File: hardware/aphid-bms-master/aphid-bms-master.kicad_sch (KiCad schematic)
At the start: 5 parts, among them J1 Main, J2 Slaves, J3 ContactorPos, J4 ContactorNeg, J5 ContactorPrecharge

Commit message: Worked on BMS master
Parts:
- added H1, H2, H3, H4: MountingHole, MountingHole:MountingHole_3.2mm_M3, symbol Mechanical:MountingHole
- added JP1: PRIMARY, Jumper:SolderJumper-2_P1.3mm_Open_RoundedPad1.0x1.5mm, symbol Jumper:SolderJumper_2_Open
- added R9: 10k, Resistor_SMD:R_0805_2012Metric, symbol Device:R
- J4, J5: footprint (none) -> Connector_Molex:Molex_Micro-Fit_3.0_43650-0215_1x02_P3.00mm_Vertical
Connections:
- net CAN/CAN1_HIGH: now also J1.4 (Pin_4); no longer J1.5 (Pin_5)
- net CAN/CAN1_LOW: now also J1.5 (Pin_5); no longer J1.4 (Pin_4)
- net CAN/CAN2_LOW: now also J2.4 (Pin_4); no longer J2.2 (Pin_2)
- net GND: now also R9.2
- net Slave Power/SLAVE_5V: now also J2.2 (Pin_2); no longer J2.4 (Pin_4)
- new net +3.3V: JP1.2 (B)
- new net MCU/PRIMARY: JP1.1 (A), R9.1
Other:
- sheet MCU ports: added PRIMARY; removed none
- note added: "Control wheater this is the primary (front) battery or the secondary (rear) battery. Enables having the same PCB and firmware in both."
- note added: "Daisy-chained to all slave boards with isolated CAN-transcievers. This board contains one 120 ohm termination, the last slave board has the other one."
- note added: "Precharge only used in primary (front) battery"
- company: (none) -> https://aphid-ev.se
- title: (none) -> Aphid BMS Master

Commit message: Worked on BMS master layout
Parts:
- H1, H2, H3, H4: footprint MountingHole:MountingHole_3.2mm_M3 -> MountingHole:MountingHole_4.3mm_M4
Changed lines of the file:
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@@
 			)
 		)
-		(property "Footprint" "MountingHole:MountingHole_3.2mm_M3"
+		(property "Footprint" "MountingHole:MountingHole_4.3mm_M4"
 			(at 29.21 158.75 0)
 			(effects
@@
 			)
 		)
-		(property "Footprint" "MountingHole:MountingHole_3.2mm_M3"
+		(property "Footprint" "MountingHole:MountingHole_4.3mm_M4"
 			(at 29.21 173.99 0)
 			(effects
@@
 			)
 		)
-		(property "Footprint" "MountingHole:MountingHole_3.2mm_M3"
+		(property "Footprint" "MountingHole:MountingHole_4.3mm_M4"
 			(at 29.21 168.91 0)
 			(effects
@@
 			)
 		)
-		(property "Footprint" "MountingHole:MountingHole_3.2mm_M3"
+		(property "Footprint" "MountingHole:MountingHole_4.3mm_M4"
 			(at 29.21 163.83 0)
 			(effects

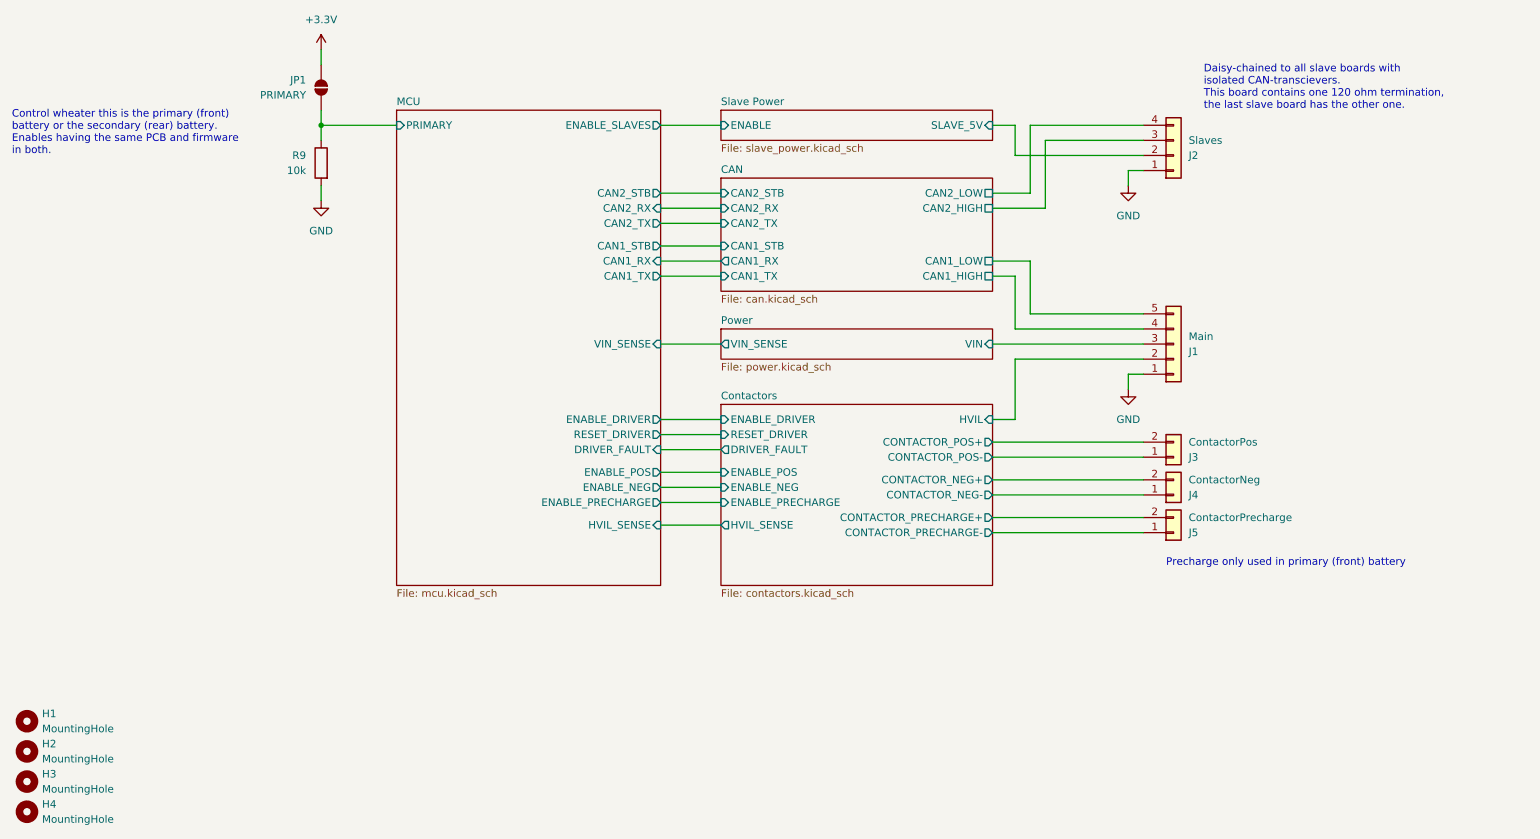
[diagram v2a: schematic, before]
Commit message: Changed BMS Master to use MAX17851 instead of isolated CAN
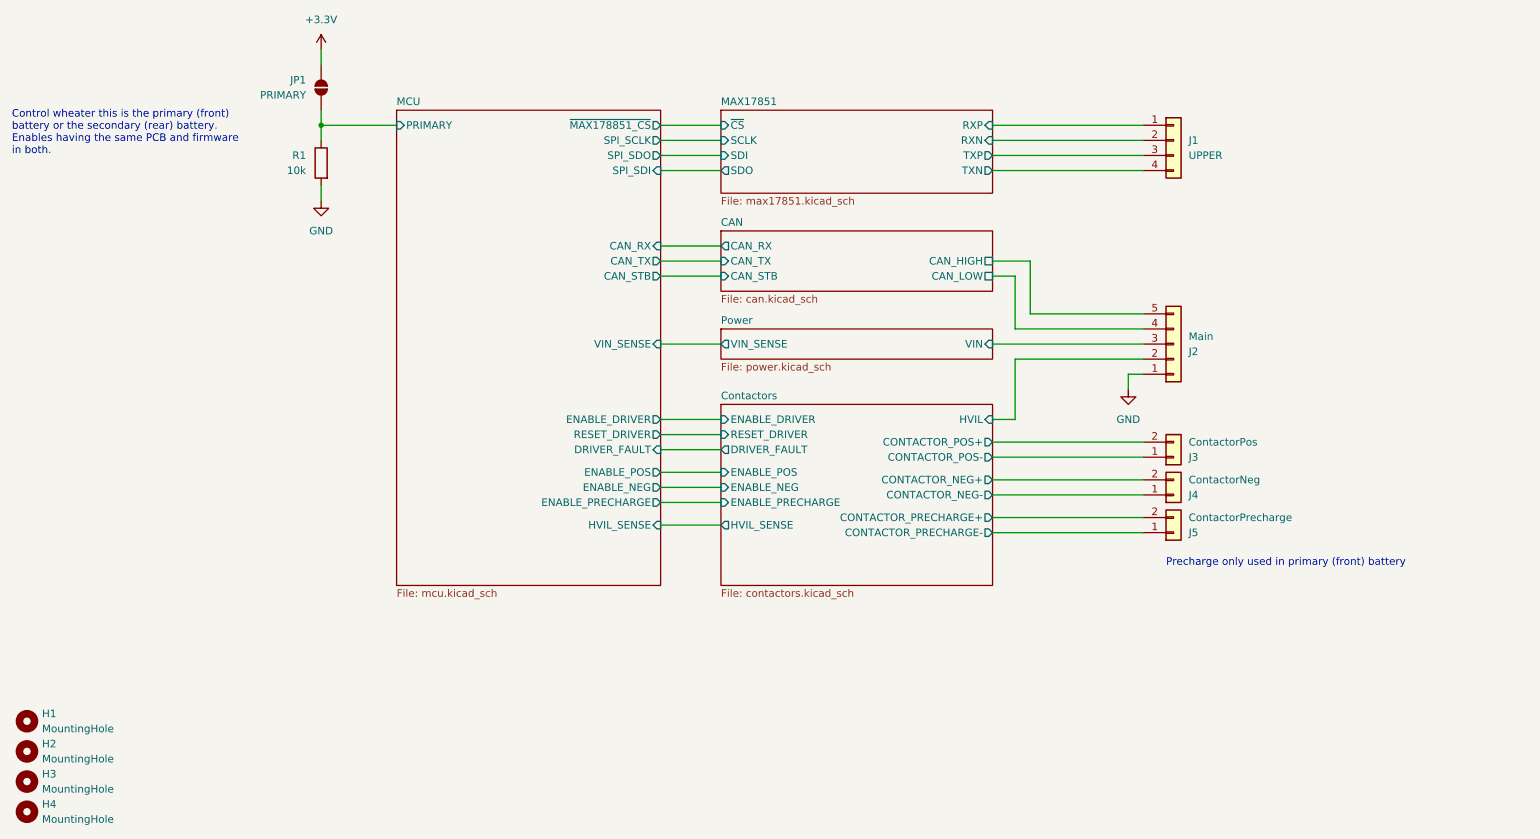
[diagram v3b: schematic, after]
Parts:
- removed J2: Slaves, Connector_Molex:Molex_Micro-Fit_3.0_43045-0412_2x02_P3.00mm_Vertical, symbol Connector_Generic:Conn_01x04
- added J1: UPPER, symbol Connector_Generic:Conn_01x04
- renumbered J1 to J2, R9 to R1
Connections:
- net CAN/CAN1_HIGH renamed CAN/CAN_LOW
- net CAN/CAN1_LOW renamed CAN/CAN_HIGH
- new net MAX17851/RXN: J1.2 (Pin_2)
- new net MAX17851/RXP: J1.1 (Pin_1)
- new net MAX17851/TXN: J1.4 (Pin_4)
- new net MAX17851/TXP: J1.3 (Pin_3)
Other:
- removed sheet Slave Power
- added sheet MAX17851 (max17851.kicad_sch)
- sheet CAN ports: added CAN_HIGH, CAN_LOW, CAN_RX, CAN_STB, CAN_TX; removed CAN1_HIGH, CAN1_LOW, CAN1_RX, CAN1_STB, CAN1_TX, CAN2_HIGH, CAN2_LOW, CAN2_RX, CAN2_STB, CAN2_TX
- sheet MCU ports: added CAN_RX, CAN_STB, CAN_TX, SPI_SCLK, SPI_SDI, SPI_SDO, ~{MAX178851_CS}; removed CAN1_RX, CAN1_STB, CAN1_TX, CAN2_RX, CAN2_STB, CAN2_TX, ENABLE_SLAVES
- note removed: "Daisy-chained to all slave boards with isolated CAN-transcievers. This board contains one 120 ohm termination, the last slave board has the other one."

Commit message: Harmonized VC and BMS components
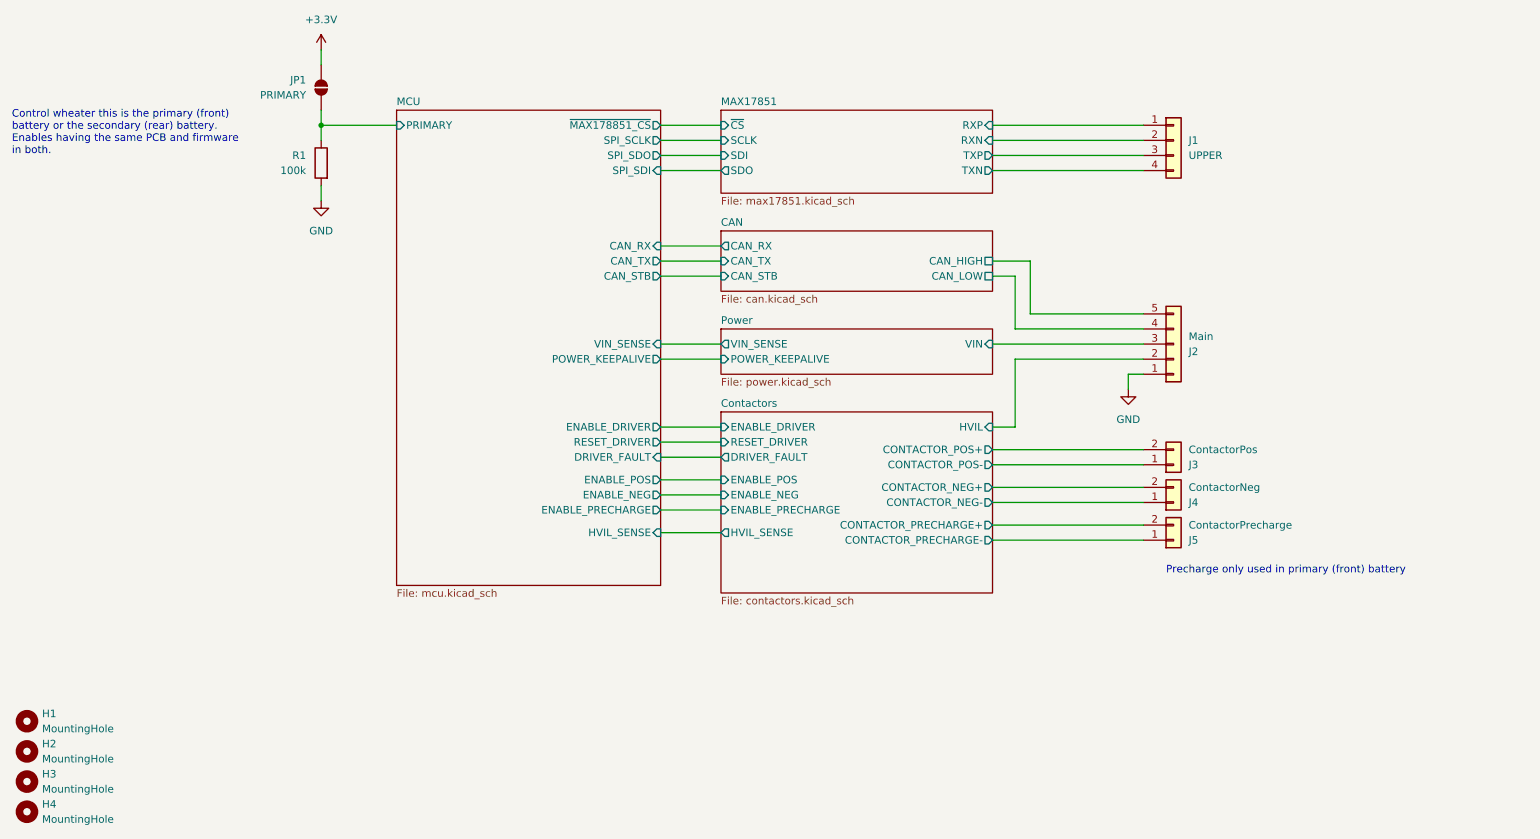
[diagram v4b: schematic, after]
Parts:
- J1: footprint (none) -> Connector_Molex:Molex_Micro-Fit_3.0_43650-0415_1x04_P3.00mm_Vertical
- R1: value 10k -> 100k
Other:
- sheet MCU ports: added POWER_KEEPALIVE; removed none
- sheet Power ports: added POWER_KEEPALIVE; removed none
- moved on the sheet: J3, J4, J5
